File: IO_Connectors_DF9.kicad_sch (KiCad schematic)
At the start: 2 parts, among them J5 DF9-41P-1V32, J6 DF9-41P-1V32

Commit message: SDRAM, bank5
last iteration of sdram. max optimization routing and space wise. Traced 2 frams to Bank 5. Fanout of bank 5 for DF9
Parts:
- removed J5, J6: DF9-41P-1V32, DataHub_Footprints:DF941P1V32, symbol DF9_connector_41:DF9-41P-1V32

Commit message: full components, LEDS, changed edges
all components on pcb editor. added and  routed leds and 2 PLL. changed edges o have more space
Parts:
- added U11: AS4C8M16SA-6TIN, DataHub_Footprints:sdram2_TSOP-54_11P96X22P35_ALL, symbol SDRAM8x16:AS4C8M16SA-6TIN
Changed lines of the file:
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@@
 	(generator_version "9.0")
 	(paper "A4")
+	(symbol
+		(lib_id "SDRAM8x16:AS4C8M16SA-6TIN")
+		(at 76.2 69.85 0)
+		(unit 1)
+		(exclude_from_sim no)
+		(in_bom yes)
+		(on_board yes)
+		(dnp no)
+		(fields_autoplaced yes)
+		(property "Reference" "U11"
+			(at 111.76 59.69 0)
+			(effects
+				(font
+					(size 1.524 1.524)
+				)
+			)
+		)
+		(property "Value" "AS4C8M16SA-6TIN"
+			(at 111.76 62.23 0)
+			(effects
+				(font
+					(size 1.524 1.524)
+				)
+			)
+		)
+		(property "Footprint" "DataHub_Footprints:sdram2_TSOP-54_11P96X22P35_ALL"
+			(at 76.2 69.85 0)
+			(effects
+				(font
+					(size 1.27 1.27)
+					(italic yes)
+				)
+				(hide yes)
+			)
+		)
+		(property "Datasheet" "AS4C8M16SA-6TIN"
+			(at 76.2 69.85 0)
+			(effects
+				(font
+					(size 1.27 1.27)
+					(italic yes)
+				)
+				(hide yes)
+			)
+		)
+		(property "Description" ""
+			(at 76.2 69.85 0)
+			(effects
+				(font
+					(size 1.27 1.27)
+				)
+				(hide yes)
+			)
+		)
+		(pin "12"
+		)
+		(pin "14"
+		)
+		(pin "3"
+		)
+		(pin "4"
+		)
+		(pin "27"
+		)
+		(pin "53"
+		)
+		(pin "16"
+		)
+		(pin "52"
+		)
+		(pin "8"
+		)
+		(pin "10"
+		)
+		(pin "1"
+		)
+		(pin "21"
+		)
+		(pin "11"
+		)
+		(pin "17"
+		)
+		(pin "15"
+		)
+		(pin "19"
+		)
+		(pin "23"
+		)
+		(pin "24"
+		)
+		(pin "6"
+		)
+		(pin "9"
+		)
+		(pin "25"
+		)
+		(pin "20"
+		)
+		(pin "7"
+		)
+		(pin "2"
+		)
+		(pin "5"
+		)
+		(pin "13"
+		)
+		(pin "18"
+		)
+		(pin "22"
+		)
+		(pin "26"
+		)
+		(pin "54"
+		)
+		(pin "50"
+		)
+		(pin "41"
+		)
+		(pin "40"
+		)
+		(pin "43"
+		)
+		(pin "42"
+		)
+		(pin "36"
+		)
+		(pin "51"
+		)
+		(pin "38"
+		)
+		(pin "32"
+		)
+		(pin "46"
+		)
+		(pin "34"
+		)
+		(pin "47"
+		)
+		(pin "33"
+		)
+		(pin "49"
+		)
+		(pin "30"
+		)
+		(pin "29"
+		)
+		(pin "37"
+		)
+		(pin "39"
+		)
+		(pin "48"
+		)
+		(pin "44"
+		)
+		(pin "31"
+		)
+		(pin "35"
+		)
+		(pin "28"
+		)
+		(pin "45"
+		)
+		(instances
+			(project ""
+				(path "/ae14ff2f-b8e3-4dd1-9329-e73906805e39/43ca8a3e-d0ec-4d1b-80e5-099bf8df79e9"
+					(reference "U11")
+					(unit 1)
+				)
+			)
+		)
+	)
 )

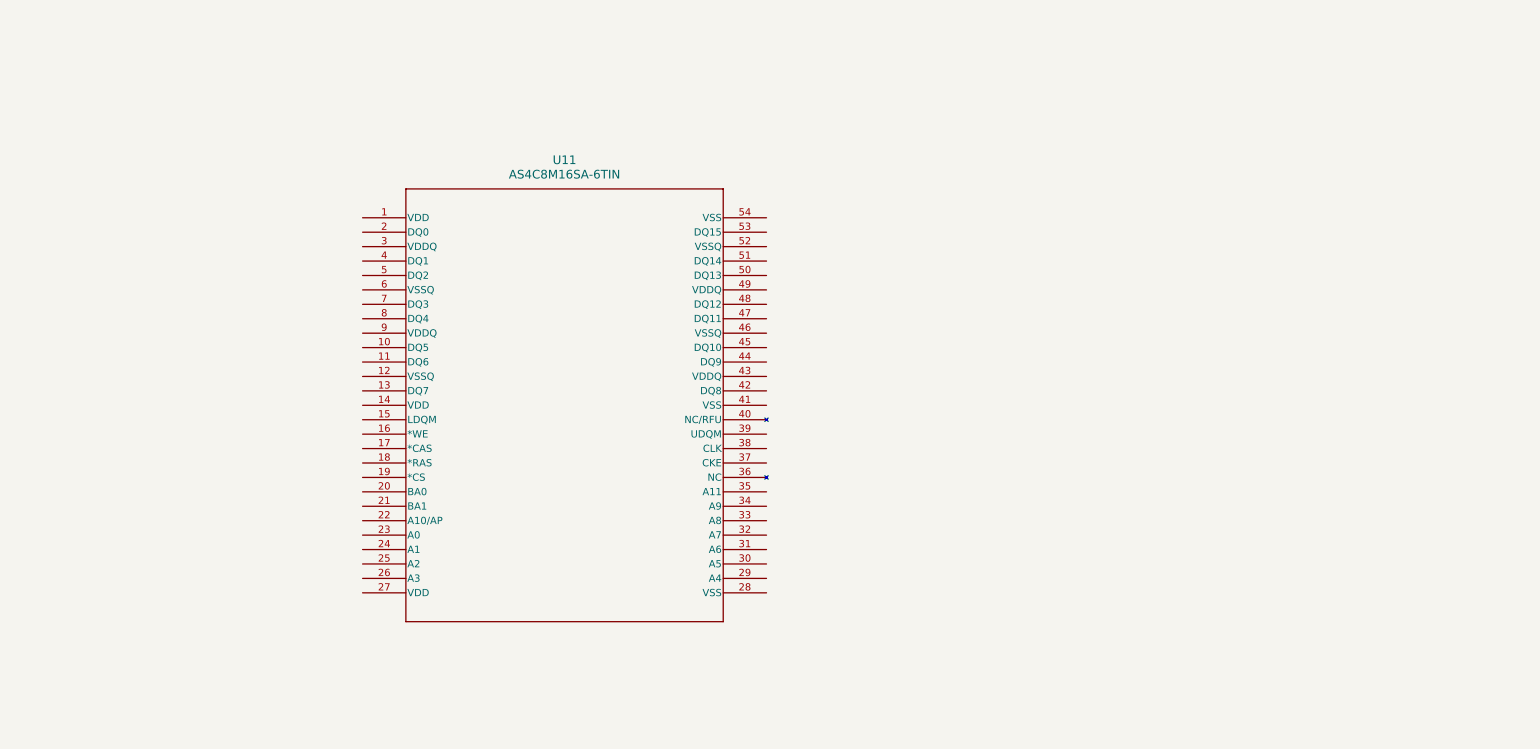
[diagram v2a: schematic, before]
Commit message: SPW Bank0
completed SPW, rotated edges and adjusted dimensions to make the extra sdram bga fit. completed Bank 0 (still to route to connector). Started fanout of bga sdram
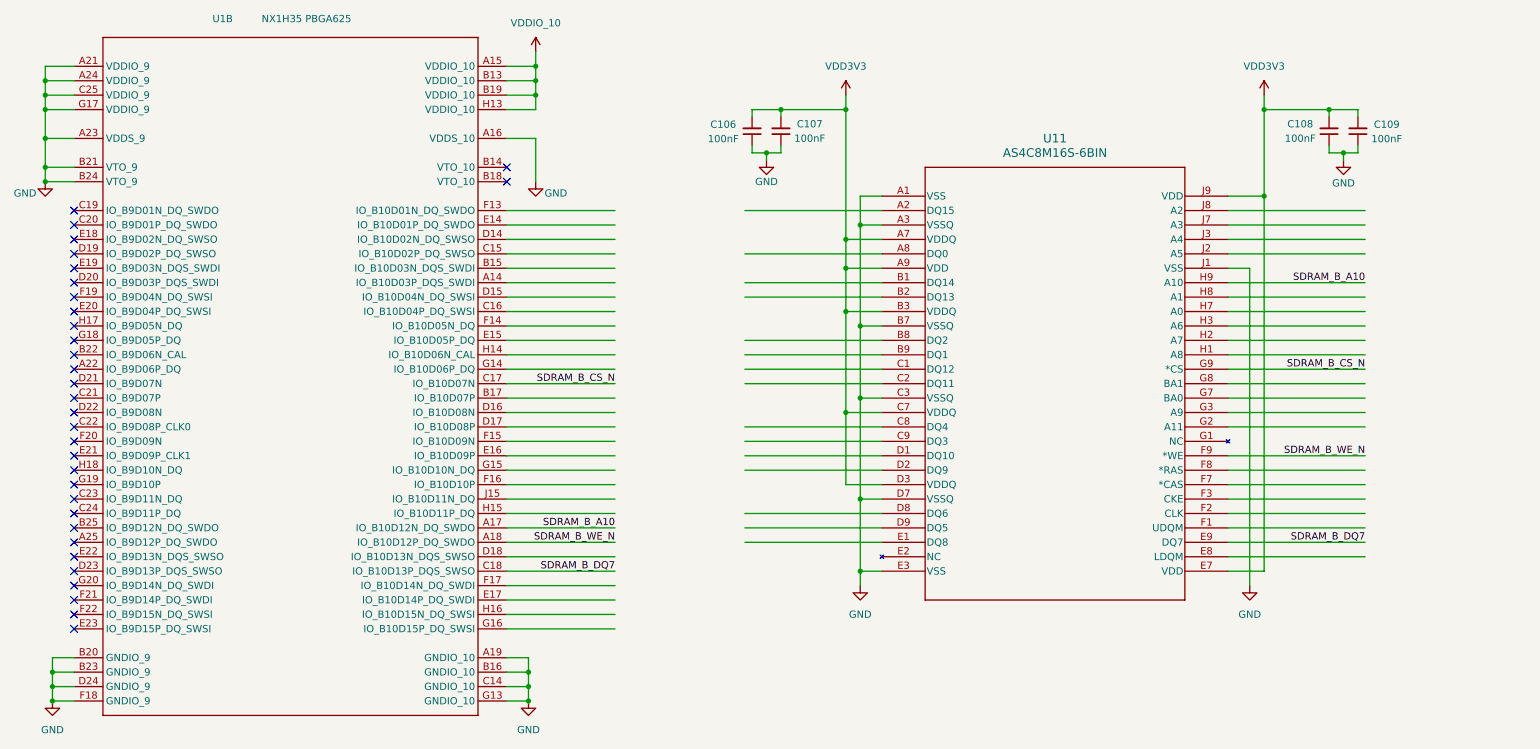
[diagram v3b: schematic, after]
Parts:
- removed U11: AS4C8M16SA-6TIN, DataHub_Footprints:sdram2_TSOP-54_11P96X22P35_ALL, symbol SDRAM8x16:AS4C8M16SA-6TIN
- added C106, C107, C108, C109: 100nF, Capacitor_SMD:C_0402_1005Metric_Pad0.74x0.62mm_HandSolder, symbol Device:C_Small
- added U1: NX1H35 PBGA625, DataHub_NG_Medium:NX1H35S_CLGA625, symbol Brave625:root_0_BRAVE625A_Brave625.SchLib
- added U11: AS4C8M16S-6BIN, DataHub_Footprints:sdram2_bga_TFBGA-54_8X8_ALL, symbol SDRAM_BGA_8x16:AS4C8M16S-6BIN
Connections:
- new net GND: C106.1, C107.1, C108.1, C109.1, U1.A16 (VDDS_10), U1.A19 (GNDIO_10), U1.A21 (VDDIO_9), U1.A23 (VDDS_9), U1.A24 (VDDIO_9), U1.B16 (GNDIO_10), U1.B20 (GNDIO_9), U1.B21 (VTO_9), U1.B23 (GNDIO_9), U1.B24 (VTO_9), U1.C14 (GNDIO_10), U1.C25 (VDDIO_9), U1.D24 (GNDIO_9), U1.F18 (GNDIO_9), U1.G13 (GNDIO_10), U1.G17 (VDDIO_9), U11.A1 (VSS), U11.A3 (VSSQ), U11.B7 (VSSQ), U11.C3 (VSSQ), U11.D7 (VSSQ), U11.E3 (VSS), U11.J1 (VSS)
- new net SDRAM_B_A10: U1.A17 (IO_B10D12N_DQ_SWDO), U11.H9 (A10)
- new net SDRAM_B_CS_N: U1.C17 (IO_B10D07N), U11.G9 (*CS)
- new net SDRAM_B_DQ7: U1.C18 (IO_B10D13P_DQS_SWSO), U11.E9 (DQ7)
- new net SDRAM_B_WE_N: U1.A18 (IO_B10D12P_DQ_SWDO), U11.F9 (*WE)
- new net VDD3V3: C106.2, C107.2, C108.2, C109.2, U11.A7 (VDDQ), U11.A9 (VDD), U11.B3 (VDDQ), U11.C7 (VDDQ), U11.D3 (VDDQ), U11.E7 (VDD), U11.J9 (VDD)
- new net VDDIO_10: U1.A15 (VDDIO_10), U1.B13 (VDDIO_10), U1.B19 (VDDIO_10), U1.H13 (VDDIO_10)
- no-connect marks 0 -> 32

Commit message: CFG, bga sdram, banks to connectors, docoupling
Finished completely routing bga sdram, finished tracing Banks to connectors DF9. Finished tracing Picoblade, diode, reset supervisor. Finished tracing LEDS on bank 5. Finished decoupling all banks and core. Missing only the power tree and power rail level decoupling.
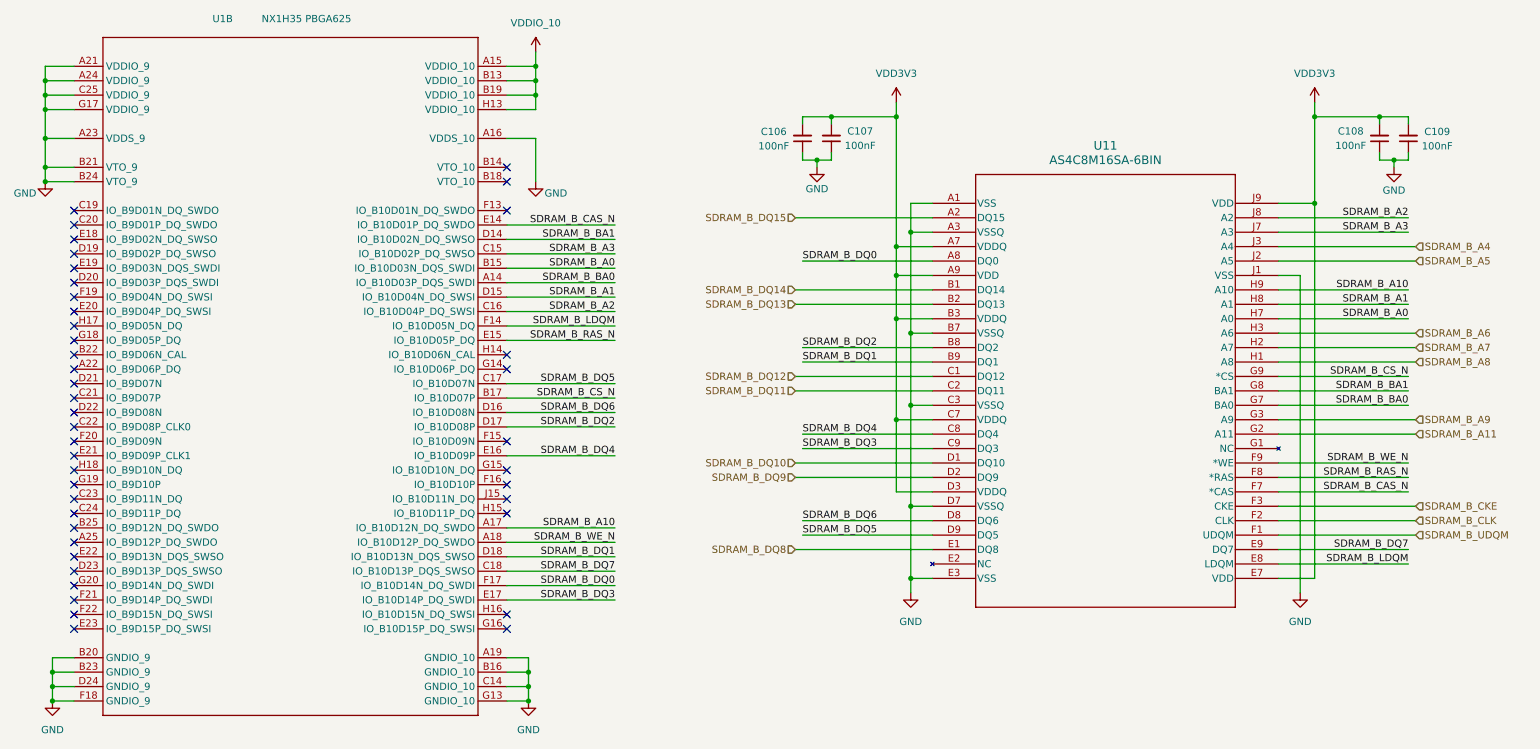
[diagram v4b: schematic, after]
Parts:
- U11: value AS4C8M16S-6BIN -> AS4C8M16SA-6BIN
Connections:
- net SDRAM_B_CS_N: now also U1.B17 (IO_B10D07P); no longer U1.C17 (IO_B10D07N)
- net SDRAM_B_DQ15: now reaches U11.A2 (DQ15)
- net SDRAM_B_DQ0: now reaches U11.A8 (DQ0)
- net SDRAM_B_DQ0: now also U1.F17 (IO_B10D14N_DQ_SWDI)
- net SDRAM_B_DQ14: now reaches U11.B1 (DQ14)
- net SDRAM_B_DQ13: now reaches U11.B2 (DQ13)
- net SDRAM_B_DQ2: now reaches U11.B8 (DQ2)
- net SDRAM_B_DQ2: now also U1.D17 (IO_B10D08P)
- net SDRAM_B_DQ1: now reaches U11.B9 (DQ1)
- net SDRAM_B_DQ1: now also U1.D18 (IO_B10D13N_DQS_SWSO)
- net SDRAM_B_DQ12: now reaches U11.C1 (DQ12)
- net SDRAM_B_DQ11: now reaches U11.C2 (DQ11)
- net SDRAM_B_DQ4: now reaches U11.C8 (DQ4)
- net SDRAM_B_DQ4: now also U1.E16 (IO_B10D09P)
- net SDRAM_B_DQ3: now reaches U11.C9 (DQ3)
- net SDRAM_B_DQ3: now also U1.E17 (IO_B10D14P_DQ_SWDI)
- net SDRAM_B_DQ10: now reaches U11.D1 (DQ10)
- net SDRAM_B_DQ9: now reaches U11.D2 (DQ9)
- net SDRAM_B_DQ6: now reaches U11.D8 (DQ6)
- net SDRAM_B_DQ6: now also U1.D16 (IO_B10D08N)
- net SDRAM_B_DQ5: now reaches U11.D9 (DQ5)
- net SDRAM_B_DQ5: now also U1.C17 (IO_B10D07N)
- net SDRAM_B_DQ8: now reaches U11.E1 (DQ8)
- net SDRAM_B_LDQM: now reaches U11.E8 (LDQM)
- net SDRAM_B_LDQM: now also U1.F14 (IO_B10D05N_DQ)
- net SDRAM_B_UDQM: now reaches U11.F1 (UDQM)
- net SDRAM_B_CLK: now reaches U11.F2 (CLK)
- net SDRAM_B_CKE: now reaches U11.F3 (CKE)
- net SDRAM_B_CAS_N: now reaches U11.F7 (*CAS)
- net SDRAM_B_CAS_N: now also U1.E14 (IO_B10D01P_DQ_SWDO)
- net SDRAM_B_RAS_N: now reaches U11.F8 (*RAS)
- net SDRAM_B_RAS_N: now also U1.E15 (IO_B10D05P_DQ)
- net SDRAM_B_A11: now reaches U11.G2 (A11)
- net SDRAM_B_A9: now reaches U11.G3 (A9)
- net SDRAM_B_BA0: now reaches U11.G7 (BA0)
- net SDRAM_B_BA0: now also U1.A14 (IO_B10D03P_DQS_SWDI)
- net SDRAM_B_BA1: now reaches U11.G8 (BA1)
- net SDRAM_B_BA1: now also U1.D14 (IO_B10D02N_DQ_SWSO)
- net SDRAM_B_A8: now reaches U11.H1 (A8)
- net SDRAM_B_A7: now reaches U11.H2 (A7)
- net SDRAM_B_A6: now reaches U11.H3 (A6)
- net SDRAM_B_A0: now reaches U11.H7 (A0)
- net SDRAM_B_A0: now also U1.B15 (IO_B10D03N_DQS_SWDI)
- net SDRAM_B_A1: now reaches U11.H8 (A1)
- net SDRAM_B_A1: now also U1.D15 (IO_B10D04N_DQ_SWSI)
- net SDRAM_B_A5: now reaches U11.J2 (A5)
- net SDRAM_B_A4: now reaches U11.J3 (A4)
- net SDRAM_B_A3: now reaches U11.J7 (A3)
- net SDRAM_B_A3: now also U1.C15 (IO_B10D02P_DQ_SWSO)
- net SDRAM_B_A2: now reaches U11.J8 (A2)
- net SDRAM_B_A2: now also U1.C16 (IO_B10D04P_DQ_SWSI)
- no-connect marks 32 -> 42
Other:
- moved on the sheet: C106, C107, C108, C109, U11

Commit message: power tree
power tree defined. Few changes remaining but almost finalized
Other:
- moved on the sheet: C106, C107, C108, C109, U11, U1B

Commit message: pre-order adjustments
DF9 connectors footprint adjusted.
Dimensions of board edges changed.
Placement of DF9 adjusted.
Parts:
- renumbered C106 to C19, C107 to C20, C108 to C24, C109 to C25, U11 to U4
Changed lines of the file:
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@@
 		(dnp no)
 		(fields_autoplaced yes)
-		(property "Reference" "#PWR0133"
+		(property "Reference" "#PWR061"
 			(at 91.948 35.56 0)
 			(effects
@@
 			(project "PCB_Project"
 				(path "/ae14ff2f-b8e3-4dd1-9329-e73906805e39/43ca8a3e-d0ec-4d1b-80e5-099bf8df79e9"
-					(reference "#PWR0133")
+					(reference "#PWR061")
 					(unit 1)
 				)
@@
 		(on_board yes)
 		(dnp no)
-		(property "Reference" "#PWR014"
+		(property "Reference" "#PWR062"
 			(at 107.95 69.85 0)
 			(effects
@@
 			(project "PCB_Project"
 				(path "/ae14ff2f-b8e3-4dd1-9329-e73906805e39/43ca8a3e-d0ec-4d1b-80e5-099bf8df79e9"
-					(reference "#PWR014")
+					(reference "#PWR062")
 					(unit 1)
 				)
@@
 		(dnp no)
 		(fields_autoplaced yes)
-		(property "Reference" "#PWR0135"
+		(property "Reference" "#PWR069"
 			(at 173.99 142.24 0)
 			(effects
@@
 			(project "PCB_Project"
 				(path "/ae14ff2f-b8e3-4dd1-9329-e73906805e39/43ca8a3e-d0ec-4d1b-80e5-099bf8df79e9"
-					(reference "#PWR0135")
+					(reference "#PWR069")
 					(unit 1)
 				)
@@
 		(on_board yes)
 		(dnp no)
-		(property "Reference" "#PWR0140"
+		(property "Reference" "#PWR081"
 			(at 259.08 67.31 0)
 			(effects
@@
 			(project "PCB_Project"
 				(path "/ae14ff2f-b8e3-4dd1-9329-e73906805e39/43ca8a3e-d0ec-4d1b-80e5-099bf8df79e9"
-					(reference "#PWR0140")
+					(reference "#PWR081")
 					(unit 1)
 				)
@@
 		(dnp no)
 		(fields_autoplaced yes)
-		(property "Reference" "U11"
+		(property "Reference" "U4"
 			(at 208.28 57.15 0)
 			(effects
@@
 			(project ""
 				(path "/ae14ff2f-b8e3-4dd1-9329-e73906805e39/43ca8a3e-d0ec-4d1b-80e5-099bf8df79e9"
-					(reference "U11")
+					(reference "U4")
 					(unit 1)
 				)
@@
 		(on_board yes)
 		(dnp no)
-		(property "Reference" "#PWR0137"
+		(property "Reference" "#PWR067"
 			(at 157.48 67.31 0)
 			(effects
@@
 			(project "PCB_Project"
 				(path "/ae14ff2f-b8e3-4dd1-9329-e73906805e39/43ca8a3e-d0ec-4d1b-80e5-099bf8df79e9"
-					(reference "#PWR0137")
+					(reference "#PWR067")
 					(unit 1)
 				)
@@
 		(on_board yes)
 		(dnp no)
-		(property "Reference" "#PWR031"
+		(property "Reference" "#PWR056"
 			(at 21.59 69.85 0)
 			(effects
@@
 			(project "PCB_Project"
 				(path "/ae14ff2f-b8e3-4dd1-9329-e73906805e39/43ca8a3e-d0ec-4d1b-80e5-099bf8df79e9"
-					(reference "#PWR031")
+					(reference "#PWR056")
 					(unit 1)
 				)
@@
 		(on_board yes)
 		(dnp no)
-		(property "Reference" "C109"
+		(property "Reference" "C25"
 			(at 266.6937 54.6883 0)
 			(effects
@@
 			(project "PCB_Project"
 				(path "/ae14ff2f-b8e3-4dd1-9329-e73906805e39/43ca8a3e-d0ec-4d1b-80e5-099bf8df79e9"
-					(reference "C109")
+					(reference "C25")
 					(unit 1)
 				)
@@
 		(dnp no)
 		(fields_autoplaced yes)
-		(property "Reference" "#PWR016"
+		(property "Reference" "#PWR057"
 			(at 22.86 161.29 0)
 			(effects
@@
 			(project "PCB_Project"
 				(path "/ae14ff2f-b8e3-4dd1-9329-e73906805e39/43ca8a3e-d0ec-4d1b-80e5-099bf8df79e9"
-					(reference "#PWR016")
+					(reference "#PWR057")
 					(unit 1)
 				)
@@
 		(on_board yes)
 		(dnp no)
-		(property "Reference" "C106"
+		(property "Reference" "C19"
 			(at 149.8663 54.6883 0)
 			(effects
@@
 			(project "PCB_Project"
 				(path "/ae14ff2f-b8e3-4dd1-9329-e73906805e39/43ca8a3e-d0ec-4d1b-80e5-099bf8df79e9"
-					(reference "C106")
+					(reference "C19")
 					(unit 1)
 				)
@@
 		(on_board yes)
 		(dnp no)
-		(property "Reference" "C107"
+		(property "Reference" "C20"
 			(at 165.0937 54.61 0)
 			(effects
@@
 			(project "PCB_Project"
 				(path "/ae14ff2f-b8e3-4dd1-9329-e73906805e39/43ca8a3e-d0ec-4d1b-80e5-099bf8df79e9"
-					(reference "C107")
+					(reference "C20")
 					(unit 1)
 				)
@@
 		(dnp no)
 		(fields_autoplaced yes)
-		(property "Reference" "#PWR0138"
+		(property "Reference" "#PWR068"
 			(at 155.448 44.45 0)
 			(effects
@@
 			(project "PCB_Project"
 				(path "/ae14ff2f-b8e3-4dd1-9329-e73906805e39/43ca8a3e-d0ec-4d1b-80e5-099bf8df79e9"
-					(reference "#PWR0138")
+					(reference "#PWR068")
 					(unit 1)
 				)
@@
 		(dnp no)
 		(fields_autoplaced yes)
-		(property "Reference" "#PWR015"
+		(property "Reference" "#PWR060"
 			(at 106.68 161.29 0)
 			(effects
@@
 			(project "PCB_Project"
 				(path "/ae14ff2f-b8e3-4dd1-9329-e73906805e39/43ca8a3e-d0ec-4d1b-80e5-099bf8df79e9"
-					(reference "#PWR015")
+					(reference "#PWR060")
 					(unit 1)
 				)
@@
 		(dnp no)
 		(fields_autoplaced yes)
-		(property "Reference" "#PWR0136"
+		(property "Reference" "#PWR076"
 			(at 242.57 142.24 0)
 			(effects
@@
 			(project "PCB_Project"
 				(path "/ae14ff2f-b8e3-4dd1-9329-e73906805e39/43ca8a3e-d0ec-4d1b-80e5-099bf8df79e9"
-					(reference "#PWR0136")
+					(reference "#PWR076")
 					(unit 1)
 				)
@@
 		(dnp no)
 		(fields_autoplaced yes)
-		(property "Reference" "#PWR0139"
+		(property "Reference" "#PWR078"
 			(at 229.108 44.45 0)
 			(effects
@@
 			(project "PCB_Project"
 				(path "/ae14ff2f-b8e3-4dd1-9329-e73906805e39/43ca8a3e-d0ec-4d1b-80e5-099bf8df79e9"
-					(reference "#PWR0139")
+					(reference "#PWR078")
 					(unit 1)
 				)
@@
 		(on_board yes)
 		(dnp no)
-		(property "Reference" "C108"
+		(property "Reference" "C24"
 			(at 251.4663 54.61 0)
 			(effects
@@
 			(project "PCB_Project"
 				(path "/ae14ff2f-b8e3-4dd1-9329-e73906805e39/43ca8a3e-d0ec-4d1b-80e5-099bf8df79e9"
-					(reference "C108")
+					(reference "C24")
 					(unit 1)
 				)
@@
 					(reference "U1")
 					(unit 2)
-				)
-				(path "/ae14ff2f-b8e3-4dd1-9329-e73906805e39/77861c37-88e9-4408-9723-ec14cfd3d63b"
-					(reference "U1")
-					(unit 2)
